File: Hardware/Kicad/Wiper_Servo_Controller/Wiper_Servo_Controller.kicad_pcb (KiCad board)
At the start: 6 copper layers, 175 x 130 mm, 66 parts, among them J1 Conn_01x04, J10 DMX, J11 Conn_02x04_Odd_Even, J12 Conn_02x04_Odd_Even, J13 Screw_Terminal_01x08, J14 12-24V in, J15 Screw_Terminal_01x08, J2 Conn_01x04, J3 Conn_01x04, J4 Conn_02x04_Odd_Even, J5 Conn_02x04_Odd_Even, J6 Conn_02x04_Odd_Even, J7 Conn_02x04_Odd_Even, J8 Conn_02x04_Odd_Even, J9 Conn_02x04_Odd_Even, U1 DRV8871, U10 DRV8871, U2 DRV8871, U3 DRV8871, U4 DRV8871, U5 LM1117T-3.3, U6 DRV8871, U7 DRV8871, U9 DRV8871

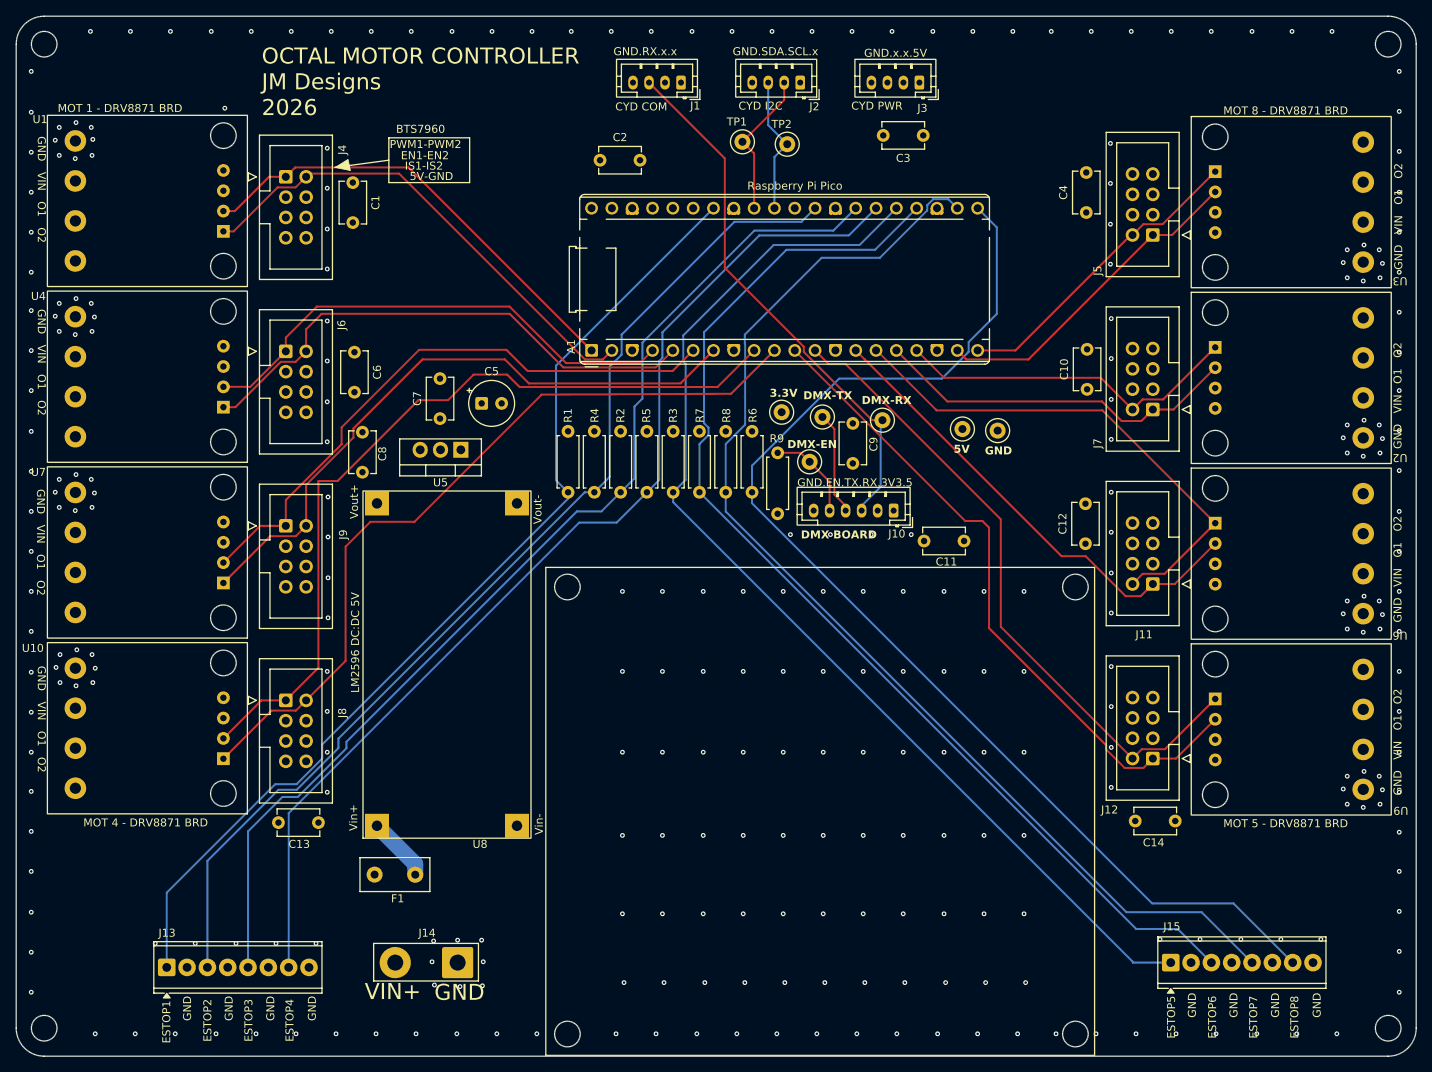
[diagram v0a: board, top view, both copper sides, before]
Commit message: Switch from DMX to RS485
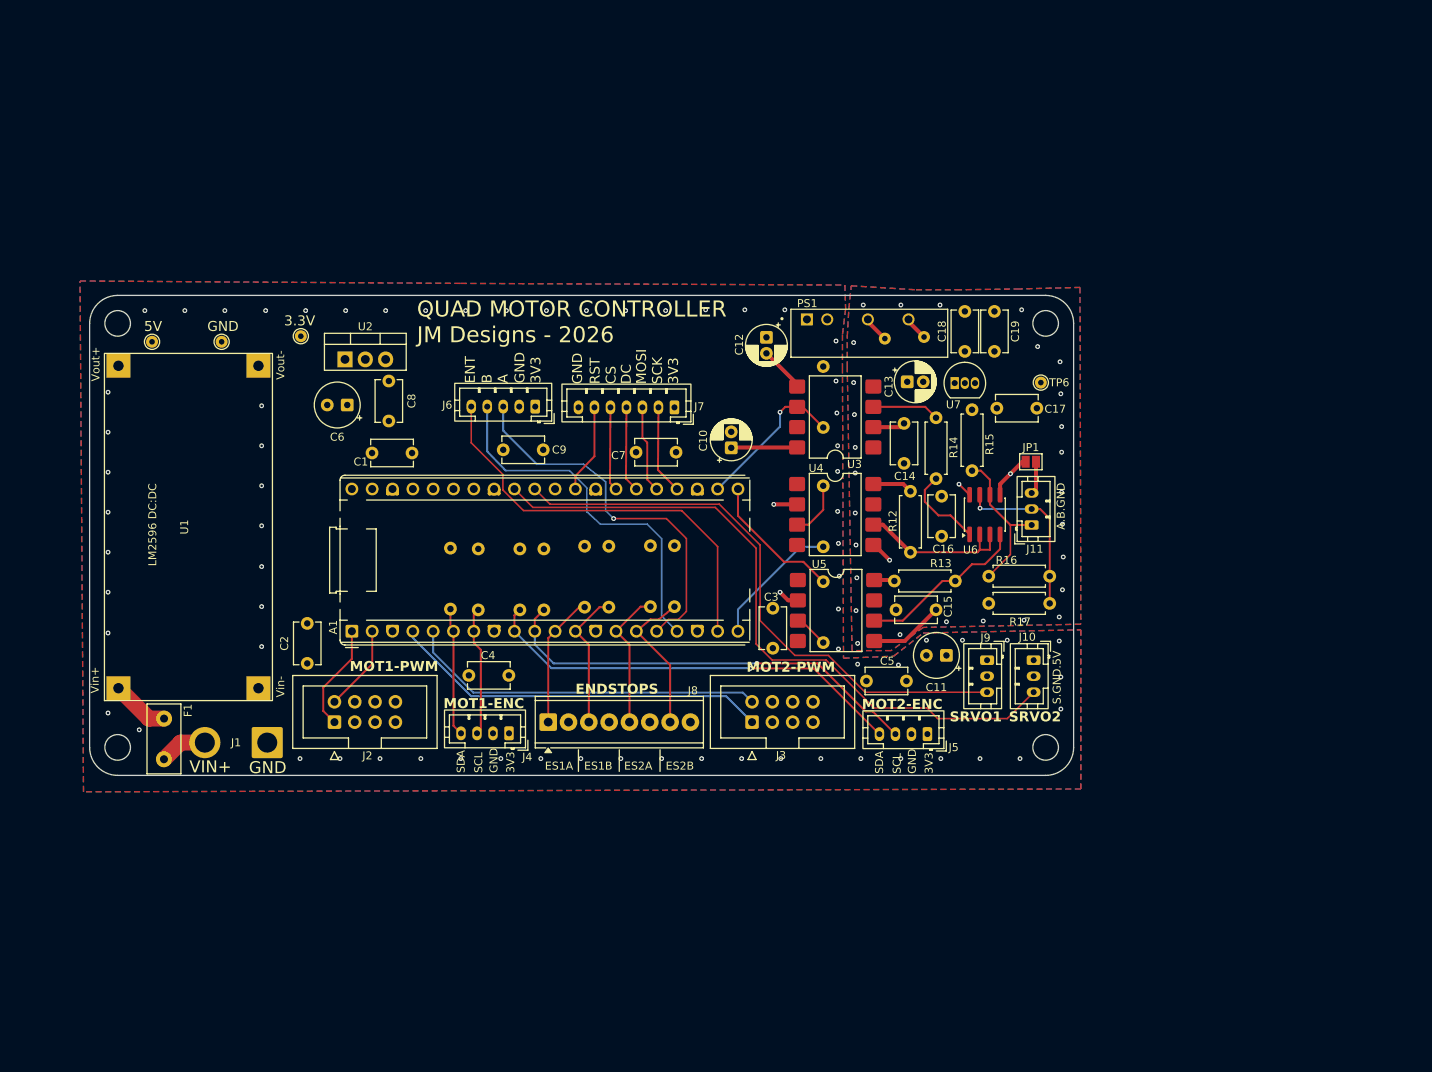
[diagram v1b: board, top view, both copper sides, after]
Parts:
- removed H5, H6, H7, H8: MountingHole, MountingHole:MountingHole_3.2mm_M3
- removed J12: Conn_02x04_Odd_Even, Connector_IDC:IDC-Header_2x04_P2.54mm_Vertical
- removed J13, J15: Screw_Terminal_01x08, TerminalBlock_Phoenix:TerminalBlock_Phoenix_MPT-0,5-8-2.54_1x08_P2.54mm_Horizontal
- removed J14: 12-24V in, Connector_Wire:SolderWire-2sqmm_1x02_P7.8mm_D2mm_OD3.9mm
- removed TP7: 3.3V, TestPoint:TestPoint_Loop_D2.50mm_Drill1.0mm
- removed TP8: GND, TestPoint:TestPoint_Loop_D2.50mm_Drill1.0mm
- removed U10, U9: DRV8871, 1_Joe_Footprints:DRV8871_Brd
- removed U8: ~, 1_Joe_Footprints:DCDC_Converter_LM2596_3A
- added C15: 0.1uF, Capacitor_THT:C_Disc_D5.1mm_W3.2mm_P5.00mm, F.Cu at (167.1, 102.3)
- added C16: 0.1uF, Capacitor_THT:C_Disc_D5.1mm_W3.2mm_P5.00mm, F.Cu at (172.8, 88.1)
- added C17: 0.1uF, Capacitor_THT:C_Disc_D5.1mm_W3.2mm_P5.00mm, F.Cu at (179.7, 77.1)
- added C18: 1uF, Capacitor_THT:C_Disc_D5.1mm_W3.2mm_P5.00mm, F.Cu at (175.7, 70.0)
- added C19: 1uF, Capacitor_THT:C_Disc_D5.1mm_W3.2mm_P5.00mm, F.Cu at (179.4, 70.0)
- added JP1: Shield, Jumper:SolderJumper-2_P1.3mm_Open_Pad1.0x1.5mm, F.Cu at (183.9, 83.8)
- added PS1: RFB-0505S, RFB-0505S:CONV_RFB-0505S, F.Cu at (163.8, 67.7)
- added R10: 330, Resistor_THT:R_Axial_DIN0207_L6.3mm_D2.5mm_P7.62mm_Horizontal, B.Cu at (158.0, 86.8)
- added R11: 330, Resistor_THT:R_Axial_DIN0207_L6.3mm_D2.5mm_P7.62mm_Horizontal, B.Cu at (158.0, 106.4)
- added R12: 470, Resistor_THT:R_Axial_DIN0207_L6.3mm_D2.5mm_P7.62mm_Horizontal, F.Cu at (168.9, 95.1)
- added R13: 470, Resistor_THT:R_Axial_DIN0207_L6.3mm_D2.5mm_P7.62mm_Horizontal, F.Cu at (174.5, 98.7)
- added R14: 470, Resistor_THT:R_Axial_DIN0207_L6.3mm_D2.5mm_P7.62mm_Horizontal, F.Cu at (172.1, 85.9)
- added R15: 680, Resistor_THT:R_Axial_DIN0207_L6.3mm_D2.5mm_P7.62mm_Horizontal, F.Cu at (176.6, 84.9)
- added R16: 120, Resistor_THT:R_Axial_DIN0207_L6.3mm_D2.5mm_P7.62mm_Horizontal, F.Cu at (186.3, 98.1)
- added R17: 680, Resistor_THT:R_Axial_DIN0207_L6.3mm_D2.5mm_P7.62mm_Horizontal, F.Cu at (178.7, 101.5)
- C10: value 0.1uF -> 10uF 10V; footprint Capacitor_THT:C_Disc_D5.1mm_W3.2mm_P5.00mm -> Capacitor_THT:CP_Radial_D5.0mm_P2.00mm
- C11, C6: value 0.1uF -> 10uF-T; footprint Capacitor_THT:C_Disc_D5.1mm_W3.2mm_P5.00mm -> Capacitor_THT:CP_Radial_Tantal_D5.5mm_P2.50mm
- C12, C13: value 0.1uF -> 4.7uF; footprint Capacitor_THT:C_Disc_D5.1mm_W3.2mm_P5.00mm -> Capacitor_THT:CP_Radial_D5.0mm_P2.00mm
- C5: value 10uF-T -> 0.1uF; footprint Capacitor_THT:CP_Radial_Tantal_D5.5mm_P2.50mm -> Capacitor_THT:C_Disc_D5.1mm_W3.2mm_P5.00mm
- J1: value Conn_01x04 -> 12-24V in; footprint Connector_JST:JST_PH_B4B-PH-K_1x04_P2.00mm_Vertical -> Connector_Wire:SolderWire-2sqmm_1x02_P7.8mm_D2mm_OD3.9mm
- J10: value DMX -> Servo2; footprint Connector_JST:JST_PH_B6B-PH-K_1x06_P2.00mm_Vertical -> Connector_JST:JST_PH_B3B-PH-K_1x03_P2.00mm_Vertical
- J11: value Conn_02x04_Odd_Even -> RS485; footprint Connector_IDC:IDC-Header_2x04_P2.54mm_Vertical -> Connector_JST:JST_PH_B3B-PH-K_1x03_P2.00mm_Vertical
- J2, J3: value Conn_01x04 -> Conn_02x04_Odd_Even; footprint Connector_JST:JST_PH_B4B-PH-K_1x04_P2.00mm_Vertical -> Connector_IDC:IDC-Header_2x04_P2.54mm_Vertical
- J4: value Conn_02x04_Odd_Even -> Mot 1 Enc; footprint Connector_IDC:IDC-Header_2x04_P2.54mm_Vertical -> Connector_JST:JST_PH_B4B-PH-K_1x04_P2.00mm_Vertical
- J5: value Conn_02x04_Odd_Even -> Mot 2 Enc; footprint Connector_IDC:IDC-Header_2x04_P2.54mm_Vertical -> Connector_JST:JST_PH_B4B-PH-K_1x04_P2.00mm_Vertical
- J6: value Conn_02x04_Odd_Even -> UI Inputs; footprint Connector_IDC:IDC-Header_2x04_P2.54mm_Vertical -> Connector_JST:JST_PH_B5B-PH-K_1x05_P2.00mm_Vertical
- J7: value Conn_02x04_Odd_Even -> SPI TFT; footprint Connector_IDC:IDC-Header_2x04_P2.54mm_Vertical -> Connector_JST:JST_PH_B7B-PH-K_1x07_P2.00mm_Vertical
- J8: value Conn_02x04_Odd_Even -> Screw_Terminal_01x08; footprint Connector_IDC:IDC-Header_2x04_P2.54mm_Vertical -> TerminalBlock_Phoenix:TerminalBlock_Phoenix_MPT-0,5-8-2.54_1x08_P2.54mm_Horizontal
- J9: value Conn_02x04_Odd_Even -> Servo1; footprint Connector_IDC:IDC-Header_2x04_P2.54mm_Vertical -> Connector_JST:JST_PH_B3B-PH-K_1x03_P2.00mm_Vertical
- R1, R2, R3, R4: value 10K -> 2.2K; moved to B.Cu
- R5, R6, R7, R8: moved to B.Cu
- R9: value 10K -> 470; moved to B.Cu
- TP1: value TestPoint -> 5V; footprint TestPoint:TestPoint_Loop_D2.50mm_Drill1.0mm -> TestPoint:TestPoint_THTPad_D1.5mm_Drill0.7mm
- TP2: value TestPoint -> 3.3V; footprint TestPoint:TestPoint_Loop_D2.50mm_Drill1.0mm -> TestPoint:TestPoint_THTPad_D1.5mm_Drill0.7mm
- TP3: value DMX_RX -> GND; footprint TestPoint:TestPoint_Loop_D2.50mm_Drill1.0mm -> TestPoint:TestPoint_THTPad_D1.5mm_Drill0.7mm
- TP4: value TestPoint -> DMX_RX; footprint TestPoint:TestPoint_Loop_D2.50mm_Drill1.0mm -> TestPoint:TestPoint_THTPad_D1.5mm_Drill0.7mm; moved to B.Cu
- TP5: footprint TestPoint:TestPoint_Loop_D2.50mm_Drill1.0mm -> TestPoint:TestPoint_THTPad_D1.5mm_Drill0.7mm; moved to B.Cu
- TP6: value 5V -> ~; footprint TestPoint:TestPoint_Loop_D2.50mm_Drill1.0mm -> TestPoint:TestPoint_THTPad_D1.5mm_Drill0.7mm
- U1: value DRV8871 -> DCDC 5V; footprint 1_Joe_Footprints:DRV8871_Brd -> 1_Joe_Footprints:DCDC_Converter_LM2596_3A
- U2: value DRV8871 -> LM1117T-3.3; footprint 1_Joe_Footprints:DRV8871_Brd -> Package_TO_SOT_THT:TO-220-3_Vertical
- U3, U4: value DRV8871 -> 6N137; footprint 1_Joe_Footprints:DRV8871_Brd -> Package_DIP:SMDIP-8_W9.53mm
- U5: value LM1117T-3.3 -> 6N137; footprint Package_TO_SOT_THT:TO-220-3_Vertical -> Package_DIP:SMDIP-8_W9.53mm
- U6: value DRV8871 -> MAX3485; footprint 1_Joe_Footprints:DRV8871_Brd -> Package_SO:SOIC-8_3.9x4.9mm_P1.27mm
- U7: value DRV8871 -> MCP1700-3302ETO; footprint 1_Joe_Footprints:DRV8871_Brd -> Package_TO_SOT_THT:TO-92_Inline
- moved H2 181.5 mm to (69.8, 119.5)
- moved U2 106.1 mm to (98.2, 71.0)
- moved J2 98.9 mm to (96.9, 116.3), turned to 90 degrees
- moved J1 97.4 mm to (88.5, 118.9)
- moved C13 96.0 mm to (168.5, 73.8)
- moved U7 94.0 mm to (174.4, 74.0), turned to 0 degrees
- moved C4 92.5 mm to (118.7, 110.5), turned to 180 degrees
- moved J9 89.3 mm to (178.5, 108.6), turned to -90 degrees
- moved TP3 83.2 mm to (82.8, 68.8), turned to 0 degrees
- moved J3 82.6 mm to (149.1, 116.3), turned to 90 degrees
- moved TP1 77.9 mm to (74.1, 68.8), turned to 0 degrees
- moved J4 74.9 mm to (118.7, 117.7), turned to 180 degrees
- moved U4 73.8 mm to (159.5, 90.4), turned to 0 degrees
- moved C2 72.8 mm to (93.5, 109.0), turned to 90 degrees
- moved J5 68.5 mm to (171.0, 117.8)
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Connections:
- A1 pad 10: /MOT_4_PWM_2 -> /MOT_2_ENC_SCL
- A1 pad 11: /MOT_5_PWM_1 -> /MOT_1_ESTOP_A
- A1 pad 12: /MOT_5_PWM_2 -> /MOT_1_ESTOP_B
- A1 pad 14: /MOT_6_PWM_1 -> /MOT_2_ESTOP_A
- A1 pad 15: /MOT_6_PWM_2 -> /MOT_2_ESTOP_B
- A1 pad 16: /MOT_7_PWM_1 -> /UI_ENC_A
- A1 pad 17: /MOT_7_PWM_2 -> /UI_ENC_B
- A1 pad 19: /MOT_8_PWM_1 -> /UI_BUTTON
- A1 pad 20: /MOT_8_PWM_2 -> /RS485_DE_TTL
- A1 pad 21: /MOT_8_ENDSTOP -> /RS485_TX_TTL
- A1 pad 22: /MOT_7_ENDSTOP -> /RS485_RX_TTL
- A1 pad 24: /MOT_6_ENDSTOP -> /DISP_SCK
- A1 pad 25: /MOT_5_ENDSTOP -> /DISP_MOSI
- A1 pad 26: /MOT_4_ENDSTOP -> /DISP_DC
- A1 pad 27: /MOT_3_ENDSTOP -> /DISP_CS
- A1 pad 29: /MOT_2_ENDSTOP -> /DISP_RST
- A1 pad 31: /I2C_SDA -> /SERVO_0
- A1 pad 32: /I2C_SCL -> /SERVO_1
- A1 pad 34: /MOT_1_ENDSTOP -> unconnected-(A1-GPIO28_ADC2-Pad34)
- A1 pad 6: /MOT_3_PWM_1 -> /MOT_1_ENC_SDA
- A1 pad 7: /MOT_3_PWM_2 -> /MOT_1_ENC_SCL
- A1 pad 9: /MOT_4_PWM_1 -> /MOT_2_ENC_SDA
- C10 pad 1: 5V -> 3.3V
- C13 pad 1: 5V -> +5V_ISO
- C13 pad 2: GND -> GND_ISO
- C14 pad 1: 5V -> +5V_ISO
- C14 pad 2: GND -> GND_ISO
- C4 pad 1: 5V -> 3.3V
- C6 pad 1: 5V -> 3.3V
- C8 pad 1: 5V -> 3.3V
- F1 pad 2: Net-(U8-Vin+) -> Net-(U1-Vin+)
- J1 pad 1: unconnected-(J1-Pin_1-Pad1) -> GND
- J1 pad 2: unconnected-(J1-Pin_2-Pad2) -> VIN
- J10 pad 2: 3.3V -> GND
- J10 pad 3: /DMX_RX_TTL -> /SERVO_1
- J11 pad 1: /MOT_6_PWM_1 -> RS485_A
- J11 pad 2: /MOT_6_PWM_2 -> RS485_B
- J11 pad 3: 5V -> Net-(J11-Pin_3)
- J2 pad 1: unconnected-(J2-Pin_1-Pad1) -> /MOT_1_PWM_1
- J2 pad 2: /I2C_SCL -> /MOT_1_PWM_2
- J2 pad 3: /I2C_SDA -> 5V
- J2 pad 4: GND -> 5V
- J3 pad 1: 5V -> /MOT_2_PWM_1
- J3 pad 2: unconnected-(J3-Pin_2-Pad2) -> /MOT_2_PWM_2
- J3 pad 3: unconnected-(J3-Pin_3-Pad3) -> 5V
- J3 pad 4: GND -> 5V
- J4 pad 1: /MOT_1_PWM_1 -> 3.3V
- J4 pad 2: /MOT_1_PWM_2 -> GND
- J4 pad 3: 5V -> /MOT_1_ENC_SCL
- J4 pad 4: 5V -> /MOT_1_ENC_SDA
- J5 pad 1: /MOT_8_PWM_1 -> 3.3V
- J5 pad 2: /MOT_8_PWM_2 -> GND
- J5 pad 3: 5V -> /MOT_2_ENC_SCL
- J5 pad 4: 5V -> /MOT_2_ENC_SDA
- J6 pad 1: /MOT_2_PWM_1 -> 3.3V
- J6 pad 2: /MOT_2_PWM_2 -> GND
- J6 pad 3: 5V -> /UI_ENC_A
- J6 pad 4: 5V -> /UI_ENC_B
- J6 pad 5: unconnected-(J6-Pin_5-Pad5) -> /UI_BUTTON
- J7 pad 1: /MOT_7_PWM_1 -> 3.3V
- J7 pad 2: /MOT_7_PWM_2 -> /DISP_SCK
- J7 pad 3: 5V -> /DISP_MOSI
- J7 pad 4: 5V -> /DISP_DC
- J7 pad 5: unconnected-(J7-Pin_5-Pad5) -> /DISP_CS
- J7 pad 6: unconnected-(J7-Pin_6-Pad6) -> /DISP_RST
- J7 pad 7: 5V -> GND
- J8 pad 1: /MOT_4_PWM_1 -> /MOT_1_ESTOP_A
- J8 pad 2: /MOT_4_PWM_2 -> GND
- J8 pad 3: 5V -> /MOT_1_ESTOP_B
- J8 pad 4: 5V -> GND
- J8 pad 5: unconnected-(J8-Pin_5-Pad5) -> /MOT_2_ESTOP_A
- J8 pad 6: unconnected-(J8-Pin_6-Pad6) -> GND
- J8 pad 7: 5V -> /MOT_2_ESTOP_B
- J9 pad 1: /MOT_3_PWM_1 -> 5V
- J9 pad 2: /MOT_3_PWM_2 -> GND
- J9 pad 3: 5V -> /SERVO_0
- R1 pad 1: /MOT_1_ENDSTOP -> /MOT_1_ENC_SDA
- R2 pad 1: /MOT_3_ENDSTOP -> /MOT_2_ENC_SDA
- R3 pad 1: /MOT_5_ENDSTOP -> /MOT_1_ENC_SCL
- R4 pad 1: /MOT_2_ENDSTOP -> /MOT_2_ENC_SCL
- R5 pad 1: /MOT_4_ENDSTOP -> /MOT_2_ESTOP_B
- R6 pad 1: /MOT_8_ENDSTOP -> /MOT_2_ESTOP_A
- R7 pad 1: /MOT_6_ENDSTOP -> /MOT_1_ESTOP_B
- R8 pad 1: /MOT_7_ENDSTOP -> /MOT_1_ESTOP_A
- R9 pad 1: GND -> 3.3V
- R9 pad 2: /DMX_EN_TTL -> /RS485_RX_TTL
- TP1 pad 1: /I2C_SCL -> 5V
- TP2 pad 1: /I2C_SDA -> 3.3V
- TP3 pad 1: /DMX_RX_TTL -> GND
- TP4 pad 1: /DMX_EN_TTL -> +5V_ISO
- TP5 pad 1: /DMX_TX_TTL -> GND_ISO
- TP6 pad 1: 5V -> +3.3V_ISO
- U1 pad 1: /MOT_1_PWM_2 -> GND
- U1 pad 2: /MOT_1_PWM_1 -> Net-(U1-Vin+)
- U1 pad 3: unconnected-(U1-VM-Pad3) -> GND
- U1 pad 4: GND -> 5V
- U2 pad 1: /MOT_7_PWM_2 -> GND
- U2 pad 2: /MOT_7_PWM_1 -> 3.3V
- U2 pad 3: unconnected-(U2-VM-Pad3) -> 5V
- U3 pad 1: /MOT_8_PWM_2 -> unconnected-(U3-NC-Pad1)
- U3 pad 2: /MOT_8_PWM_1 -> +5V_ISO
- U3 pad 3: unconnected-(U3-VM-Pad3) -> Net-(U3-C)
- U3 pad 4: GND -> unconnected-(U3-NC-Pad4)
- U3 pad 6: VIN -> /RS485_RX_TTL
- U3 pad 8: unconnected-(U3-OUT2-Pad8) -> 3.3V
- U4 pad 1: /MOT_2_PWM_2 -> unconnected-(U4-NC-Pad1)
- U4 pad 2: /MOT_2_PWM_1 -> 3.3V
- U4 pad 3: unconnected-(U4-VM-Pad3) -> Net-(U4-C)
- U4 pad 4: GND -> unconnected-(U4-NC-Pad4)
- U4 pad 5: GND -> GND_ISO
- U4 pad 6: VIN -> Net-(U4-VO)
- U4 pad 8: unconnected-(U4-OUT2-Pad8) -> +5V_ISO
- U5 pad 1: GND -> unconnected-(U5-NC-Pad1)
- U5 pad 3: 5V -> Net-(U5-C)
- U6 pad 1: /MOT_6_PWM_2 -> Net-(U6-RO)
- U6 pad 2: /MOT_6_PWM_1 -> Net-(U4-VO)
- U6 pad 3: unconnected-(U6-VM-Pad3) -> Net-(U4-VO)
- U6 pad 4: GND -> Net-(U5-VO)
- U6 pad 5: GND -> GND_ISO
- U6 pad 6: VIN -> RS485_A
- U6 pad 7: unconnected-(U6-OUT1-Pad7) -> RS485_B
- U6 pad 8: unconnected-(U6-OUT2-Pad8) -> +3.3V_ISO
- U7 pad 1: /MOT_3_PWM_2 -> GND_ISO
- U7 pad 2: /MOT_3_PWM_1 -> +5V_ISO
- U7 pad 3: unconnected-(U7-VM-Pad3) -> +3.3V_ISO
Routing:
- net /MOT_8_ENDSTOP: track 149.4 -> 0.00 mm
- net /MOT_7_ENDSTOP: track 146.7 -> 0.00 mm
- net /MOT_6_ENDSTOP: track 142.0 -> 0.00 mm
- net /MOT_5_ENDSTOP: track 140.9 -> 0.00 mm
- net /MOT_3_ENDSTOP: track 135.1 -> 0.00 mm
- net /MOT_4_ENDSTOP: track 134.6 -> 0.00 mm
- net /MOT_2_ENDSTOP: track 133.3 -> 0.00 mm
- net /MOT_1_ENDSTOP: track 126.0 -> 0.00 mm
- net /MOT_4_PWM_1: track 101.4 -> 0.00 mm
- net /MOT_4_PWM_2: track 98.3 -> 0.00 mm
- net /SERVO_1: track 0.00 -> 85.2 mm
- net /MOT_5_PWM_1: track 84.4 -> 0.00 mm
- net /MOT_5_PWM_2: track 82.1 -> 0.00 mm
- net /MOT_3_PWM_2: track 79.5 -> 0.00 mm
- net /MOT_3_PWM_1: track 75.0 -> 0.00 mm
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- added copper zone on In3.Cu, net +3.3V_ISO
- added copper zone on In2.Cu, net +5V_ISO
- added copper zone on In2.Cu, net 5V
- added copper zone on B.Cu, net GND
- added copper zone on F.Cu, net GND
- added copper zone on B.Cu, net GND_ISO
- added copper zone on F.Cu, net GND_ISO
- added copper zone on In1.Cu, net GND_ISO
- added copper zone on In4.Cu, net GND_ISO
- removed copper zone on In3.Cu, net 5V
- removed copper zone on In2.Cu, net VIN
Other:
- board size 175 x 130 mm -> 123 x 60 mm
- board text added: "3V3"
- board text added: "5VISO"
- board text added: "A"
- board text added: "A.B.GND"
- board text added: "B"
- board text added: "CS"
- board text added: "DC"
- board text added: "ENDSTOPS"
- board text added: "ENT"
- board text added: "ES1A"
- board text added: "ES1B"
- board text added: "ES2A"
- board text added: "ES2B"
- board text added: "GNDISO"
- board text added: "MOSI"
- board text added: "MOT1-ENC"
- board text added: "MOT1-PWM"
- board text added: "MOT2-ENC"
- board text added: "MOT2-PWM"
- board text added: "QUAD MOTOR CONTROLLER JM Designs - 2026"
- board text added: "RST"
- board text added: "S.GND.5V"
- board text added: "SCK"
- board text added: "SCL"
- board text added: "SDA"
- board text added: "SRVO1"
- board text added: "SRVO2"
- board text removed: "5V-GND"
- board text removed: "BTS7960"
- board text removed: "CYD COM"
- board text removed: "CYD I2C"
- board text removed: "CYD PWR"
- board text removed: "DMX BOARD"
- board text removed: "DMX-EN"
- board text removed: "DMX-RX"
- board text removed: "DMX-TX"
- board text removed: "EN1-EN2"
- board text removed: "ESTOP1"
- board text removed: "ESTOP2"
- board text removed: "ESTOP3"
- board text removed: "ESTOP4"
- board text removed: "ESTOP5"
- board text removed: "ESTOP6"
- board text removed: "ESTOP7"
- board text removed: "ESTOP8"
- board text removed: "GND VIN O1 O2"
- board text removed: "GND.EN.TX.RX.3V3.5"
- board text removed: "GND.RX.x.x"
- board text removed: "GND.SDA.SCL.x"
- board text removed: "GND.x.x.5V"
- board text removed: "IS1-IS2"
- board text removed: "MOT 1 - DRV8871 BRD"
- board text removed: "MOT 4 - DRV8871 BRD"
- board text removed: "MOT 5 - DRV8871 BRD"
- board text removed: "MOT 8 - DRV8871 BRD"
- board text removed: "OCTAL MOTOR CONTROLLER JM Designs 2026"
- board text removed: "PWM1-PWM2"
- board text removed: "Raspberry Pi Pico"
